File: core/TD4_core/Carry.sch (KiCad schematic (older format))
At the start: 4 parts

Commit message: Started refactoring
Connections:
- net nRESET renamed ~RESET
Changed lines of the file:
@@
 EESchema Schematic File Version 4
+LIBS:TD4_core-cache
 EELAYER 26 0
 EELAYER END
@@
 encoding utf-8
 Sheet 6 6
-Title ""
+Title "TD4 core module"
 Date ""
-Rev ""
+Rev "v1.0"
 Comp ""
 Comment1 ""
@@
 	5750 3350 5750 3450
 Wire Wire Line
-	5750 3450 5200 3450
-Wire Wire Line
-	5200 3450 5200 3350
-Wire Wire Line
-	5200 3350 4950 3350
+	5750 3450 4950 3450
 Text HLabel 4950 2950 0    50   Input ~ 0
 C_in
-Text HLabel 4950 3150 0    50   Input ~ 0
-CLK
-Text HLabel 4950 3350 0    50   Input ~ 0
-nRESET
 Text HLabel 6600 3150 2    50   Input ~ 0
 nC_out
+Text GLabel 4950 3450 0    50   Input ~ 0
+~RESET
+Text GLabel 4950 3150 0    50   Input ~ 0
+CLK
 $EndSCHEMATC

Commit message: RAM refactoring goes on
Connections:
- net nC_out renamed ~C_out
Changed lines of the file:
@@
 Text HLabel 4950 2950 0    50   Input ~ 0
 C_in
-Text HLabel 6600 3150 2    50   Input ~ 0
-nC_out
+Text HLabel 6600 3150 2    50   Output ~ 0
+~C_out
 Text GLabel 4950 3450 0    50   Input ~ 0
 ~RESET

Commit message: Core assembled; decoder left
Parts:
- gave numbers to parts that had none: 2
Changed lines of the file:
@@
 $EndDescr
 $Comp
-L 74xx:74HC74 U?
+L 74xx:74HC74 U12
 U 1 1 5C77EAC1
 P 5750 3050
-F 0 "U?" H 5750 3700 50  0000 C CNN
+F 0 "U12" H 5750 3700 50  0000 C CNN
 F 1 "74HC74" H 5750 3600 50  0000 C CNN
 F 2 "" H 5750 3050 50  0001 C CNN
@@
 $EndComp
 $Comp
-L 74xx:74HC74 U?
+L 74xx:74HC74 U12
 U 2 1 5C77EB31
 P 5750 4800
-F 0 "U?" H 5750 5400 50  0000 C CNN
+F 0 "U12" H 5750 5400 50  0000 C CNN
 F 1 "74HC74" H 5750 5300 50  0000 C CNN
 F 2 "" H 5750 4800 50  0001 C CNN
@@
 $EndComp
 $Comp
-L 74xx:74HC74 U?
+L 74xx:74HC74 U12
 U 3 1 5C77EB96
 P 9100 5650
-F 0 "U?" H 9330 5696 50  0000 L CNN
+F 0 "U12" H 9330 5696 50  0000 L CNN
 F 1 "74HC74" H 9330 5605 50  0000 L CNN
 F 2 "" H 9100 5650 50  0001 C CNN
@@
 $EndComp
 $Comp
-L Device:C C?
+L Device:C C12
 U 1 1 5C77ECAD
 P 8550 5650
-F 0 "C?" H 8665 5696 50  0000 L CNN
+F 0 "C12" H 8665 5696 50  0000 L CNN
 F 1 "100n" H 8665 5605 50  0000 L CNN
 F 2 "" H 8588 5500 50  0001 C CNN
@@
 $EndComp
 $Comp
-L power:GND #PWR?
+L power:GND #PWR0122
 U 1 1 5C77ED22
 P 8800 6250
-F 0 "#PWR?" H 8800 6000 50  0001 C CNN
+F 0 "#PWR0122" H 8800 6000 50  0001 C CNN
 F 1 "GND" H 8805 6077 50  0000 C CNN
 F 2 "" H 8800 6250 50  0001 C CNN
@@
 Connection ~ 8800 6250
 $Comp
-L power:VCC #PWR?
+L power:VCC #PWR0123
 U 1 1 5C77ED89
 P 8800 5100
-F 0 "#PWR?" H 8800 4950 50  0001 C CNN
+F 0 "#PWR0123" H 8800 4950 50  0001 C CNN
 F 1 "VCC" H 8817 5273 50  0000 C CNN
 F 2 "" H 8800 5100 50  0001 C CNN
@@
 	5250 4800 5250 4850
 $Comp
-L power:GND #PWR?
+L power:GND #PWR0124
 U 1 1 5C77F87A
 P 5250 4850
-F 0 "#PWR?" H 5250 4600 50  0001 C CNN
+F 0 "#PWR0124" H 5250 4600 50  0001 C CNN
 F 1 "GND" H 5255 4677 50  0000 C CNN
 F 2 "" H 5250 4850 50  0001 C CNN
@@
 $EndComp
 $Comp
-L power:GND #PWR?
+L power:GND #PWR0125
 U 1 1 5C77F8A8
 P 5750 5100
-F 0 "#PWR?" H 5750 4850 50  0001 C CNN
+F 0 "#PWR0125" H 5750 4850 50  0001 C CNN
 F 1 "GND" H 5755 4927 50  0000 C CNN
 F 2 "" H 5750 5100 50  0001 C CNN
@@
 Connection ~ 5250 4700
 $Comp
-L power:VCC #PWR?
+L power:VCC #PWR0126
 U 1 1 5C7802E0
 P 5750 2750
-F 0 "#PWR?" H 5750 2600 50  0001 C CNN
+F 0 "#PWR0126" H 5750 2600 50  0001 C CNN
 F 1 "VCC" H 5767 2923 50  0000 C CNN
 F 2 "" H 5750 2750 50  0001 C CNN

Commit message: Decoder done (finally!)
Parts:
- renumbered C12 to C31, U12 to U31
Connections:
- net C_out: now reaches U31.5 (Q)
- net ~C_out: no longer names the net of U31.6 (~Q)
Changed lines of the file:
@@
 $Descr A4 11693 8268
 encoding utf-8
-Sheet 6 9
+Sheet 19 23
 Title "TD4 core module"
 Date ""
@@
 $EndDescr
 $Comp
-L 74xx:74HC74 U12
+L 74xx:74HC74 U31
 U 1 1 5C77EAC1
 P 5750 3050
-F 0 "U12" H 5750 3700 50  0000 C CNN
+F 0 "U31" H 5750 3700 50  0000 C CNN
 F 1 "74HC74" H 5750 3600 50  0000 C CNN
 F 2 "" H 5750 3050 50  0001 C CNN
@@
 $EndComp
 $Comp
-L 74xx:74HC74 U12
+L 74xx:74HC74 U31
 U 2 1 5C77EB31
 P 5750 4800
-F 0 "U12" H 5750 5400 50  0000 C CNN
+F 0 "U31" H 5750 5400 50  0000 C CNN
 F 1 "74HC74" H 5750 5300 50  0000 C CNN
 F 2 "" H 5750 4800 50  0001 C CNN
@@
 $EndComp
 $Comp
-L 74xx:74HC74 U12
+L 74xx:74HC74 U31
 U 3 1 5C77EB96
 P 9100 5650
-F 0 "U12" H 9330 5696 50  0000 L CNN
+F 0 "U31" H 9330 5696 50  0000 L CNN
 F 1 "74HC74" H 9330 5605 50  0000 L CNN
 F 2 "" H 9100 5650 50  0001 C CNN
@@
 $EndComp
 $Comp
-L Device:C C12
+L Device:C C31
 U 1 1 5C77ECAD
 P 8550 5650
-F 0 "C12" H 8665 5696 50  0000 L CNN
+F 0 "C31" H 8665 5696 50  0000 L CNN
 F 1 "100n" H 8665 5605 50  0000 L CNN
 F 2 "" H 8588 5500 50  0001 C CNN
@@
 $EndComp
 $Comp
-L power:GND #PWR0122
+L power:GND #PWR0105
 U 1 1 5C77ED22
 P 8800 6250
-F 0 "#PWR0122" H 8800 6000 50  0001 C CNN
+F 0 "#PWR0105" H 8800 6000 50  0001 C CNN
 F 1 "GND" H 8805 6077 50  0000 C CNN
 F 2 "" H 8800 6250 50  0001 C CNN
@@
 Connection ~ 8800 6250
 $Comp
-L power:VCC #PWR0123
+L power:VCC #PWR0104
 U 1 1 5C77ED89
 P 8800 5100
-F 0 "#PWR0123" H 8800 4950 50  0001 C CNN
+F 0 "#PWR0104" H 8800 4950 50  0001 C CNN
 F 1 "VCC" H 8817 5273 50  0000 C CNN
 F 2 "" H 8800 5100 50  0001 C CNN
@@
 	5250 4800 5250 4850
 $Comp
-L power:GND #PWR0124
+L power:GND #PWR0102
 U 1 1 5C77F87A
 P 5250 4850
-F 0 "#PWR0124" H 5250 4600 50  0001 C CNN
+F 0 "#PWR0102" H 5250 4600 50  0001 C CNN
 F 1 "GND" H 5255 4677 50  0000 C CNN
 F 2 "" H 5250 4850 50  0001 C CNN
@@
 $EndComp
 $Comp
-L power:GND #PWR0125
+L power:GND #PWR0103
 U 1 1 5C77F8A8
 P 5750 5100
-F 0 "#PWR0125" H 5750 4850 50  0001 C CNN
+F 0 "#PWR0103" H 5750 4850 50  0001 C CNN
 F 1 "GND" H 5755 4927 50  0000 C CNN
 F 2 "" H 5750 5100 50  0001 C CNN
@@
 Connection ~ 5250 4700
 $Comp
-L power:VCC #PWR0126
+L power:VCC #PWR0101
 U 1 1 5C7802E0
 P 5750 2750
-F 0 "#PWR0126" H 5750 2600 50  0001 C CNN
+F 0 "#PWR0101" H 5750 2600 50  0001 C CNN
 F 1 "VCC" H 5767 2923 50  0000 C CNN
 F 2 "" H 5750 2750 50  0001 C CNN
@@
 	1    0    0    -1
 $EndComp
-NoConn ~ 6050 2950
 Wire Wire Line
-	6050 3150 6600 3150
+	6050 2950 6600 2950
 Wire Wire Line
 	5450 2950 4950 2950
@@
 Text HLabel 4950 2950 0    50   Input ~ 0
 C_in
-Text HLabel 6600 3150 2    50   Output ~ 0
-~C_out
+Text HLabel 6600 2950 2    50   Output ~ 0
+C_out
 Text GLabel 4950 3450 0    50   Input ~ 0
 ~RESET
 Text GLabel 4950 3150 0    50   Input ~ 0
 CLK
+NoConn ~ 6050 3150
 $EndSCHEMATC

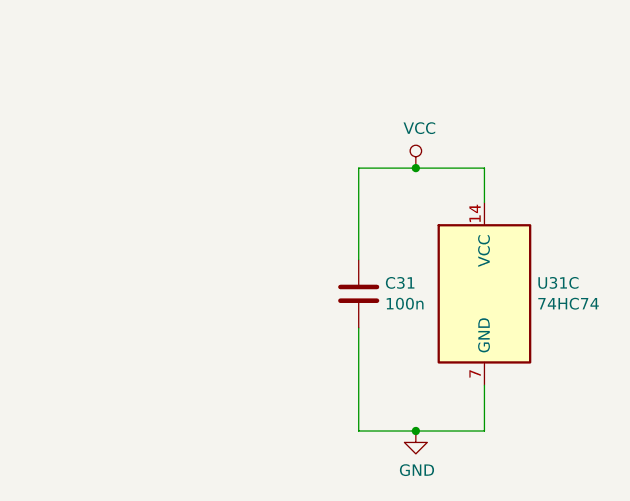
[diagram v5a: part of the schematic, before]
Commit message: Core schematic done. Backplane connector added, including separate .sch file to append.
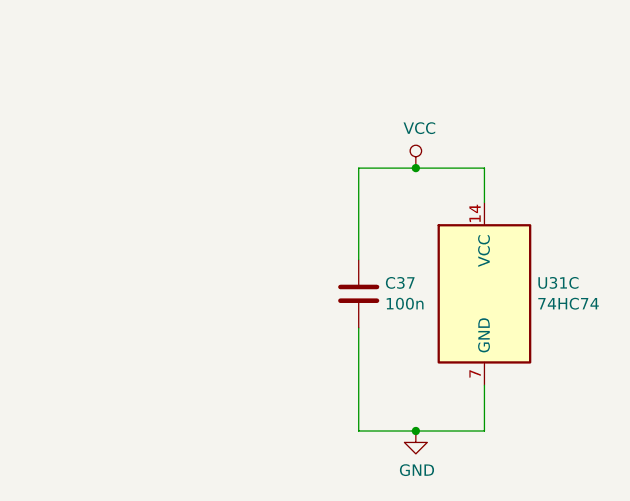
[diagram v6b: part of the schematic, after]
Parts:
- C37: renamed from C31; footprint (none) -> Capacitor_SMD:C_0805_2012Metric
- U31: footprint (none) -> Package_SO:SOIC-14_3.9x8.7mm_P1.27mm
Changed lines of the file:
@@
 F 0 "U31" H 5750 3700 50  0000 C CNN
 F 1 "74HC74" H 5750 3600 50  0000 C CNN
-F 2 "" H 5750 3050 50  0001 C CNN
+F 2 "Package_SO:SOIC-14_3.9x8.7mm_P1.27mm" H 5750 3050 50  0001 C CNN
 F 3 "74xx/74hc_hct74.pdf" H 5750 3050 50  0001 C CNN
 	1    5750 3050
@@
 F 0 "U31" H 5750 5400 50  0000 C CNN
 F 1 "74HC74" H 5750 5300 50  0000 C CNN
-F 2 "" H 5750 4800 50  0001 C CNN
+F 2 "Package_SO:SOIC-14_3.9x8.7mm_P1.27mm" H 5750 4800 50  0001 C CNN
 F 3 "74xx/74hc_hct74.pdf" H 5750 4800 50  0001 C CNN
 	2    5750 4800
@@
 F 0 "U31" H 9330 5696 50  0000 L CNN
 F 1 "74HC74" H 9330 5605 50  0000 L CNN
-F 2 "" H 9100 5650 50  0001 C CNN
+F 2 "Package_SO:SOIC-14_3.9x8.7mm_P1.27mm" H 9100 5650 50  0001 C CNN
 F 3 "74xx/74hc_hct74.pdf" H 9100 5650 50  0001 C CNN
 	3    9100 5650
@@
 $EndComp
 $Comp
-L Device:C C31
+L Device:C C37
 U 1 1 5C77ECAD
 P 8550 5650
-F 0 "C31" H 8665 5696 50  0000 L CNN
+F 0 "C37" H 8665 5696 50  0000 L CNN
 F 1 "100n" H 8665 5605 50  0000 L CNN
-F 2 "" H 8588 5500 50  0001 C CNN
+F 2 "Capacitor_SMD:C_0805_2012Metric" H 8588 5500 50  0001 C CNN
 F 3 "~" H 8550 5650 50  0001 C CNN
 	1    8550 5650
@@
 $EndComp
 $Comp
-L power:GND #PWR0105
+L power:GND #PWR0119
 U 1 1 5C77ED22
 P 8800 6250
-F 0 "#PWR0105" H 8800 6000 50  0001 C CNN
+F 0 "#PWR0119" H 8800 6000 50  0001 C CNN
 F 1 "GND" H 8805 6077 50  0000 C CNN
 F 2 "" H 8800 6250 50  0001 C CNN
@@
 Connection ~ 8800 6250
 $Comp
-L power:VCC #PWR0104
+L power:VCC #PWR0118
 U 1 1 5C77ED89
 P 8800 5100
-F 0 "#PWR0104" H 8800 4950 50  0001 C CNN
+F 0 "#PWR0118" H 8800 4950 50  0001 C CNN
 F 1 "VCC" H 8817 5273 50  0000 C CNN
 F 2 "" H 8800 5100 50  0001 C CNN
@@
 	5250 4800 5250 4850
 $Comp
-L power:GND #PWR0102
+L power:GND #PWR0116
 U 1 1 5C77F87A
 P 5250 4850
-F 0 "#PWR0102" H 5250 4600 50  0001 C CNN
+F 0 "#PWR0116" H 5250 4600 50  0001 C CNN
 F 1 "GND" H 5255 4677 50  0000 C CNN
 F 2 "" H 5250 4850 50  0001 C CNN
@@
 $EndComp
 $Comp
-L power:GND #PWR0103
+L power:GND #PWR0117
 U 1 1 5C77F8A8
 P 5750 5100
-F 0 "#PWR0103" H 5750 4850 50  0001 C CNN
+F 0 "#PWR0117" H 5750 4850 50  0001 C CNN
 F 1 "GND" H 5755 4927 50  0000 C CNN
 F 2 "" H 5750 5100 50  0001 C CNN
@@
 Connection ~ 5250 4700
 $Comp
-L power:VCC #PWR0101
+L power:VCC #PWR0115
 U 1 1 5C7802E0
 P 5750 2750
-F 0 "#PWR0101" H 5750 2600 50  0001 C CNN
+F 0 "#PWR0115" H 5750 2600 50  0001 C CNN
 F 1 "VCC" H 5767 2923 50  0000 C CNN
 F 2 "" H 5750 2750 50  0001 C CNN
